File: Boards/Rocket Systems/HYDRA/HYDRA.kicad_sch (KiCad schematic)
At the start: 63 parts, among them IC1 BC846BLT1G, IC2 NSVT30010MXV6T1G, J1 Conn_01x01_Socket, J11 Conn_01x01_Socket, J12 Conn_01x01_Socket, J13 Conn_01x01_Socket, J14 Conn_01x01_Socket, J15 Conn_01x01_Socket, J16 Conn_01x01_Socket, J17 Conn_01x01_Socket, J18 Conn_01x01_Socket, J2 Conn_01x01_Socket, J3 Conn_01x01_Socket, J4 Conn_01x01_Socket, J5 Conn_01x01_Socket, J6 Conn_01x01_Socket, J8 Conn_01x01_Socket, J9 Conn_01x01_Socket, Q2 2N7002H6327XTSA2, Q3 2N7002H6327XTSA2, Q5 BC857CMB_315, Q6 BC857CMB_315, Q7 BC857CMB_315, U12 THVD2410VDRCR, U5 SQJA36EP-T1_GE3, U6 VLMKG3400-GS08, U9 SQJA36EP-T1_GE3

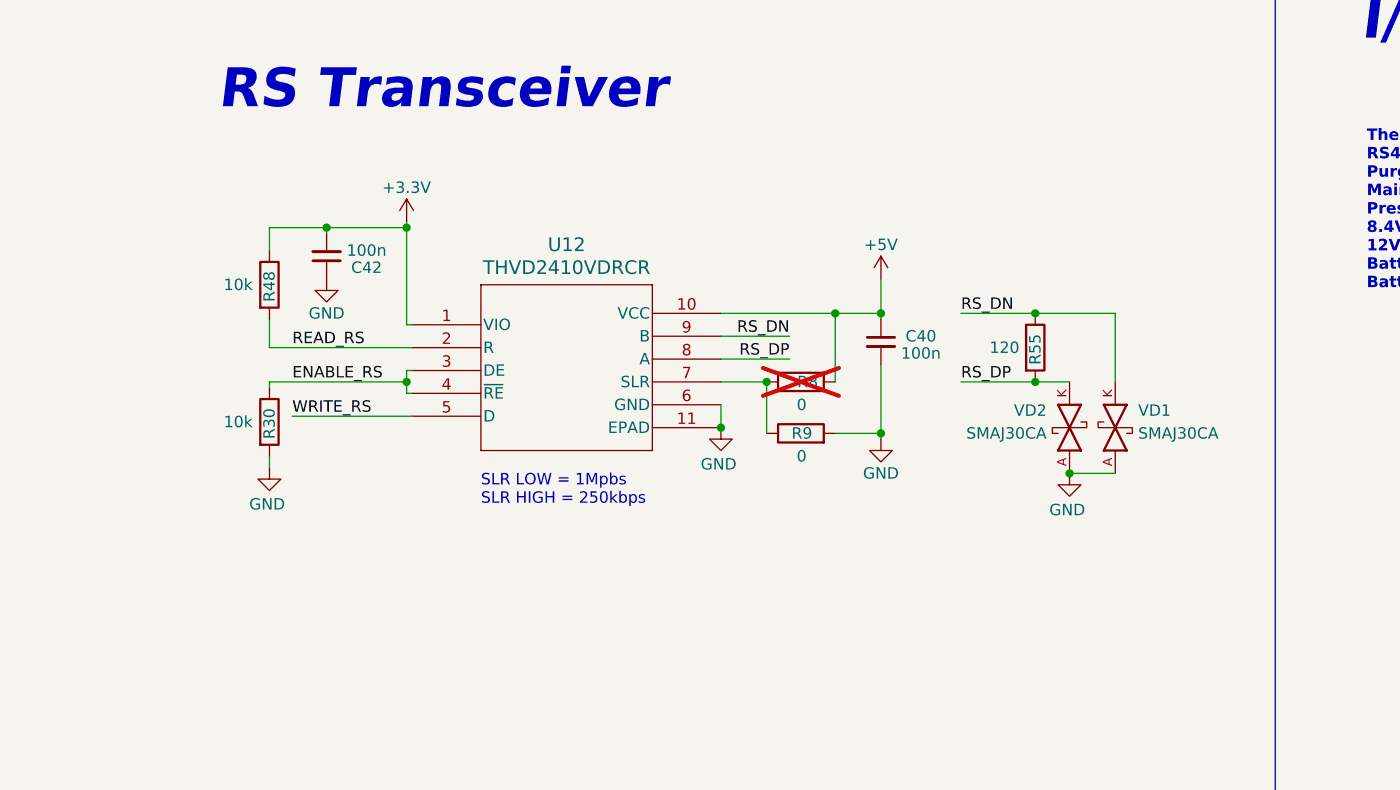
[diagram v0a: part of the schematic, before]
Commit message: OBC Full layout refactor, HYDRA Schematics UPDATE
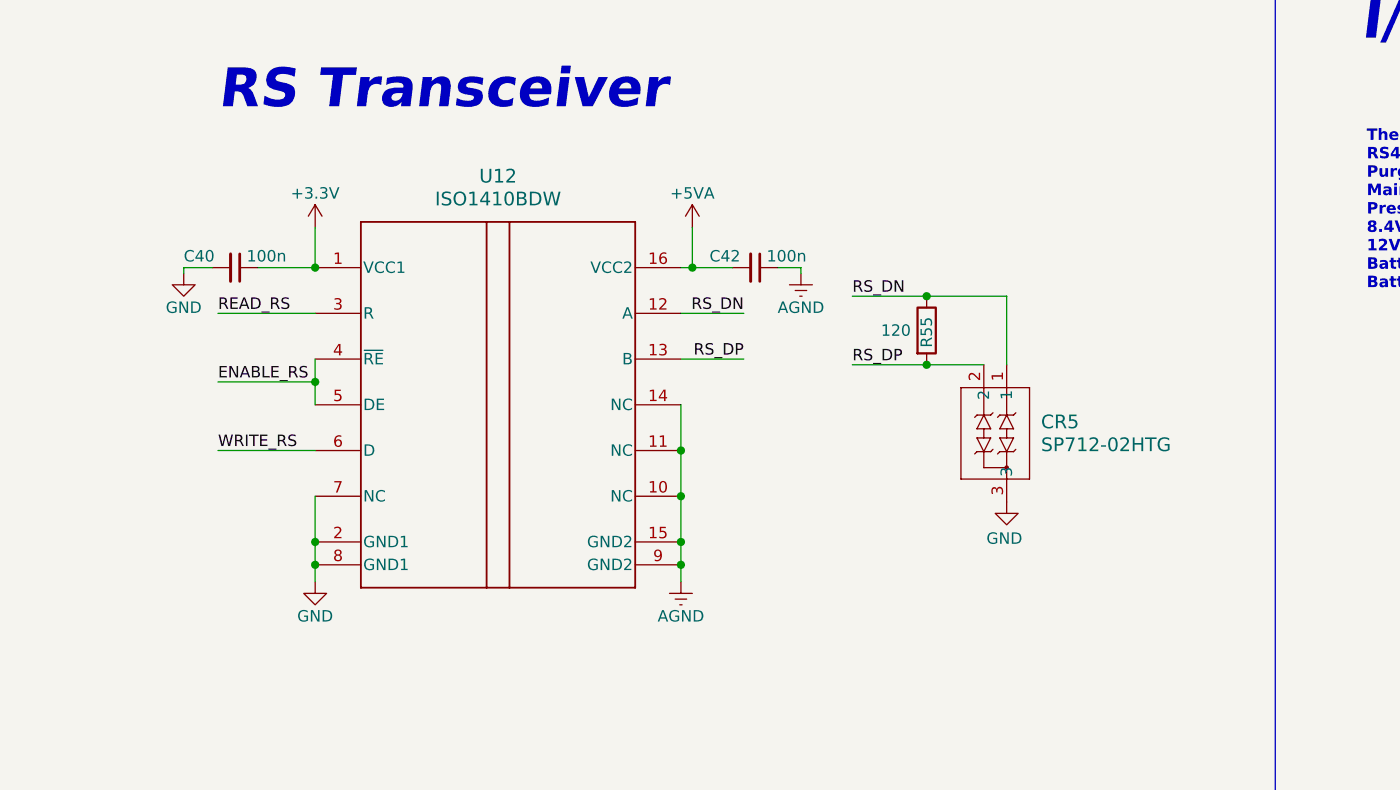
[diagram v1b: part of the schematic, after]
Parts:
- removed R30, R48: 10k, Resistor-0402:RES_0402, symbol Device:R
- removed R8, R9: 0, Resistor-0603:RES_0603, symbol Device:R
- removed U12: THVD2410VDRCR, VSON10_DRC_TEX, symbol THVD2410VDRCR:THVD2410VDRCR
- removed VD1, VD2: SMAJ30CA, symbol SMAJ30CA:SMAJ30CA
- added CR5: SP712-02HTG, 2Channel ESD RS485 - P712-02HTG:SOT23-3_LTF, symbol SP712-02HTG:SP712-02HTG
- added U12: ISO1410BDW, DW0016B_N, symbol ISO1410BDW:ISO1410BDW
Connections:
- net +3.3V: now also C40.1, U12.1 (VCC1); no longer C42.2
- net +5V: no longer C40.1
- net ENABLE_RS: now also U12.4 (~{RE}), U12.5 (DE)
- net GND: now also CR5.3, U12.2 (GND1), U12.7 (NC), U12.8 (GND1); no longer C42.1
- net READ_RS: now also U12.3 (R)
- net RS_DN: now also CR5.1, U12.12 (A)
- net RS_DP: now also CR5.2, U12.13 (B)
- net WRITE_RS: now also U12.6 (D)
- new net +5VA: C42.2, U12.16 (VCC2)
- new net AGND: C42.1, U12.10 (NC), U12.11 (NC), U12.14 (NC), U12.15 (GND2), U12.9 (GND2)
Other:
- note removed: "SLR LOW = 1Mpbs SLR HIGH = 250kbps"
- moved on the sheet: R55

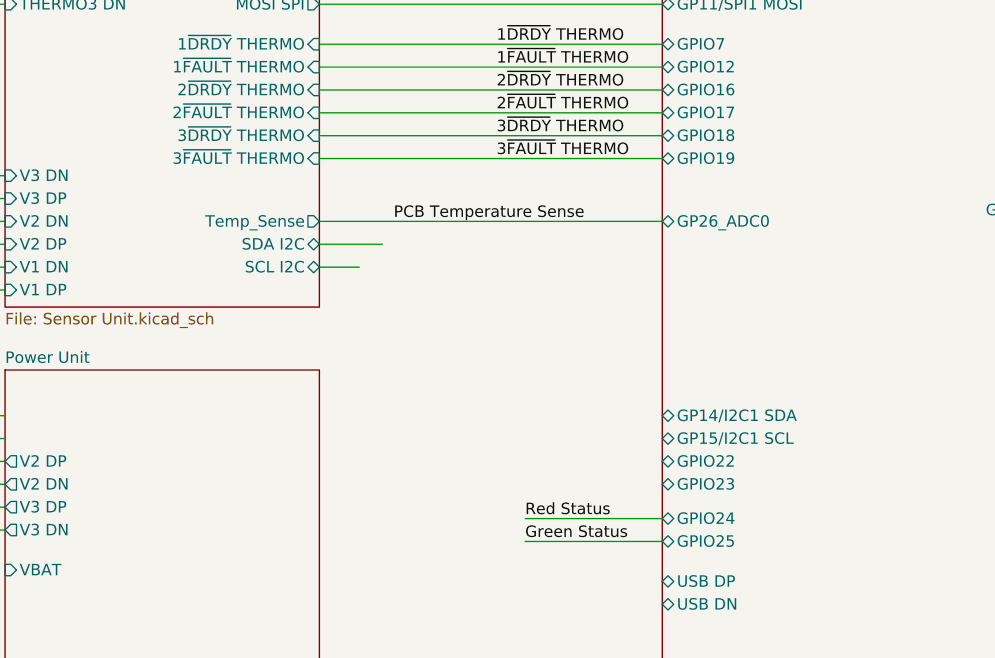
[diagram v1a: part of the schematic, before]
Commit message: updated the ADC routing in schematic
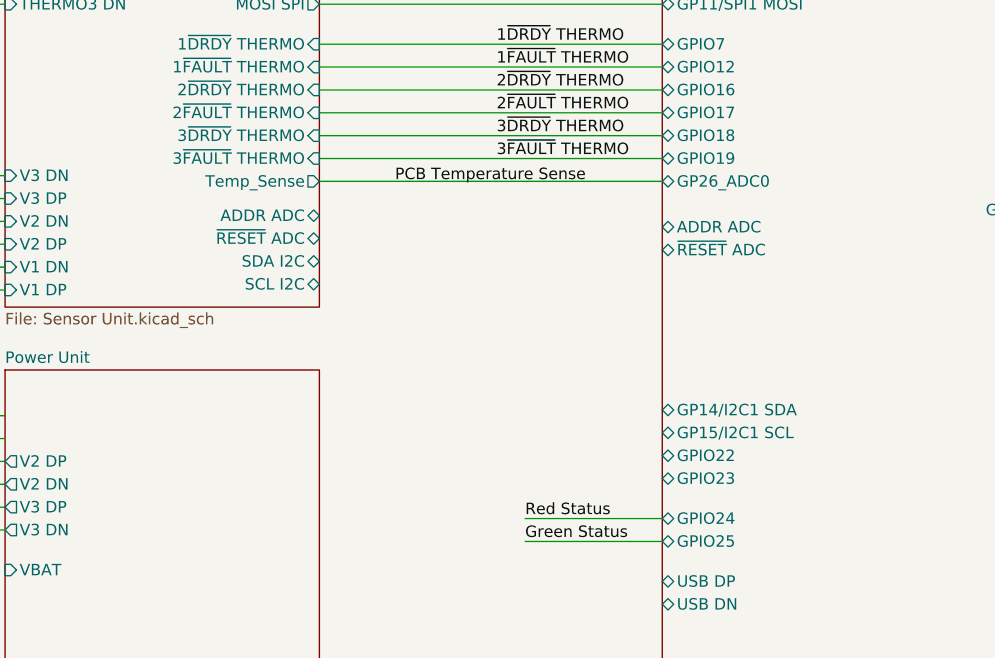
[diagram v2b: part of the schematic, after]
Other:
- sheet RP2040 Standard ports: added ADDR ADC, ~{RESET} ADC; removed none
- sheet Sensor Unit ports: added ADDR ADC, ~{RESET} ADC; removed none
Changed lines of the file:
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@@
 	(wire
 		(pts
-			(xy 100.965 100.965) (xy 105.41 100.965)
-		)
-		(stroke
-			(width 0)
-			(type default)
-		)
-	)
-	(wire
-		(pts
 			(xy 389.255 207.645) (xy 389.255 205.105)
 		)
@@
 	(wire
 		(pts
-			(xy 100.965 98.425) (xy 107.95 98.425)
-		)
-		(stroke
-			(width 0)
-			(type default)
-		)
-	)
-	(wire
-		(pts
 			(xy 251.46 74.295) (xy 251.46 79.375)
 		)
@@
 	(wire
 		(pts
-			(xy 100.965 95.885) (xy 139.065 95.885)
+			(xy 100.965 91.44) (xy 139.065 91.44)
 		)
 		(stroke
@@
 	)
 	(label "PCB Temperature Sense"
-		(at 109.22 95.885 0)
+		(at 109.3648 91.6859 0)
 		(effects
 			(font
@@
 		)
 		(pin "GPIO22" bidirectional
-			(at 139.065 122.555 180)
+			(at 139.065 121.92 180)
 			(effects
 				(font
@@
 		)
 		(pin "GP26_ADC0" bidirectional
-			(at 139.065 95.885 180)
+			(at 139.065 91.44 180)
 			(effects
 				(font
@@
 		)
 		(pin "GP15{slash}I2C1 SCL" bidirectional
-			(at 139.065 120.015 180)
+			(at 139.065 119.38 180)
 			(effects
 				(font
@@
 		)
 		(pin "GP14{slash}I2C1 SDA" bidirectional
-			(at 139.065 117.475 180)
+			(at 139.065 116.84 180)
 			(effects
 				(font
@@
 		)
 		(pin "GPIO23" bidirectional
-			(at 139.065 125.095 180)
+			(at 139.065 124.46 180)
 			(effects
 				(font
@@
 			)
 		)
+		(pin "ADDR ADC" bidirectional
+			(at 139.065 96.52 180)
+			(effects
+				(font
+					(size 1.27 1.27)
+				)
+				(justify left)
+			)
+		)
+		(pin "~{RESET} ADC" bidirectional
+			(at 139.065 99.06 180)
+			(effects
+				(font
+					(size 1.27 1.27)
+				)
+				(justify left)
+			)
+		)
 		(instances
 			(project "HYDRA"
@@
 		)
 		(pin "SDA I2C" bidirectional
-			(at 100.965 98.425 0)
+			(at 100.965 100.33 0)
 			(effects
 				(font
@@
 		)
 		(pin "SCL I2C" bidirectional
-			(at 100.965 100.965 0)
+			(at 100.965 102.87 0)
 			(effects
 				(font
@@
 		)
 		(pin "Temp_Sense" output
-			(at 100.965 95.885 0)
+			(at 100.965 91.44 0)
+			(effects
+				(font
+					(size 1.27 1.27)
+				)
+				(justify right)
+			)
+		)
+		(pin "ADDR ADC" bidirectional
+			(at 100.965 95.25 0)
+			(effects
+				(font
+					(size 1.27 1.27)
+				)
+				(justify right)
+			)
+		)
+		(pin "~{RESET} ADC" bidirectional
+			(at 100.965 97.79 0)
 			(effects
 				(font

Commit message: major changes on the HYDRA schematic including valve actuation and adc changes
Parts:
- removed D4, D7: RB095BGE-30TL, SchottkyDiode-RB095BGE:RD3P175SNFRATL, symbol RB095BGE-30TL:RB095BGE-30TL
- removed Q2, Q3: 2N7002H6327XTSA2, NMOS_2N7002:PG-SOT23-3-5_INF_MIN, symbol NMOS_2N7002:2N7002H6327XTSA2
- removed R35, R43, R57, R58: 2k, Resistor-0402:RES_0402, symbol Device:R
- removed R6, R68: 10k, Resistor-0402:RES_0402, symbol Device:R
- removed U5, U9: SQJA36EP-T1_GE3, SQJA36EP-T1-GE3:PowerPAK_SO-8L_3_VIS, symbol SQJA36EP-T1-GE3:SQJA36EP-T1_GE3
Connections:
- no-connect marks 0 -> 1
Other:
- added sheet Actuation Unit (Actuation Unit.kicad_sch)
- sheet Power Unit ports: added GNDPWR, VBAT DN, VBAT DP; removed V2 DN, V2 DP, V3 DN, V3 DP
- sheet RP2040 Standard ports: added none; removed ADDR ADC, USB DN, USB DP, ~{RESET} ADC
- sheet Sensor Unit ports: added DAC_IN1, DAC_IN2, DAC_IN3, DAC_IN4, VBAT DN, VBAT DP; removed ADDR ADC, V1 DN, V1 DP, V2 DN, V2 DP, V3 DN, V3 DP
- note added: "TODO LIST: Connectors for valves Buffer a criar Vref nos sensores de corrente Meter isto mais apresentavel Atualizar Pinout"
- note removed: "Main Valve Driver - Solenoid"
- note removed: "Purge Valve Driver - Solenoid"
- note removed: "Servo Valve Driver"
- note removed: "TODO LIST: REVER GROUNDs -> Analog, Digital, Supply LDO AGND? , USB-C PD Split AGND?, Shields nos DC.DC? Power Ground, star connection? Power Multiplexer na USB-C Buffer a criar Vref nos sensores de corrente Meter isto mais apresentavel Atualizar Pinout"
- note removed: "Valve Drivers"
- moved on the sheet: IC1, LS1, R18, R19

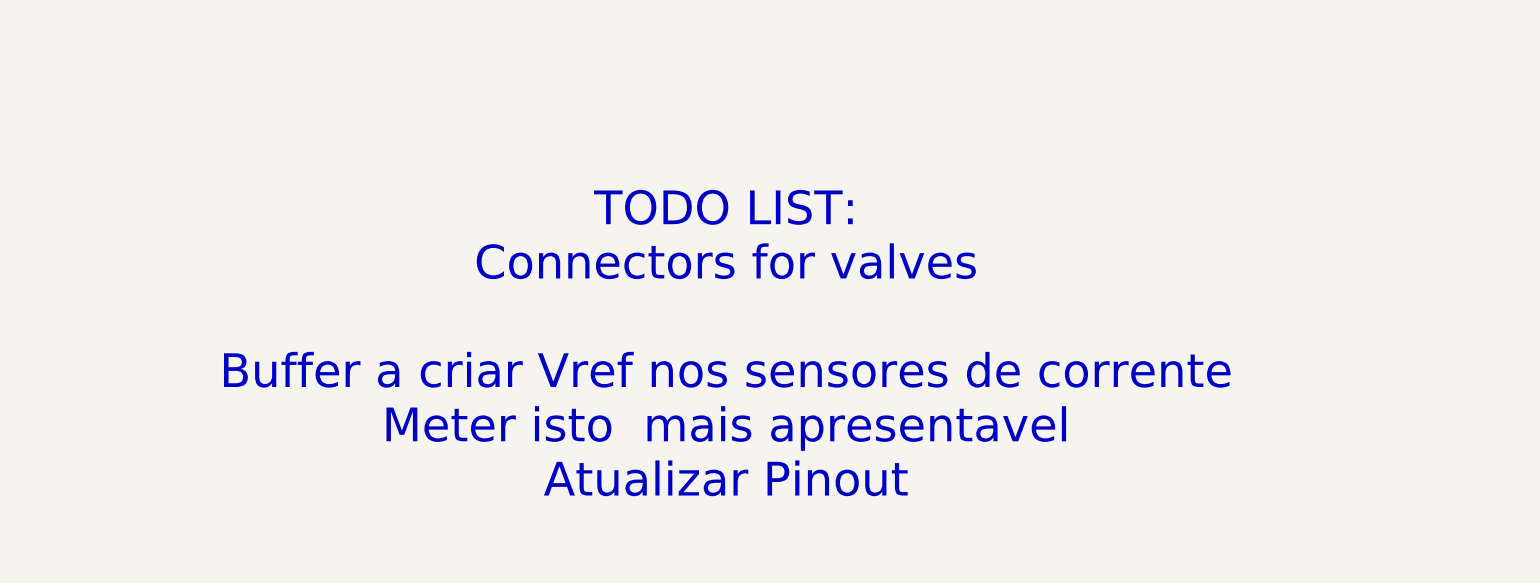
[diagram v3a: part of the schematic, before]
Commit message: Reordered the DC DC schematic
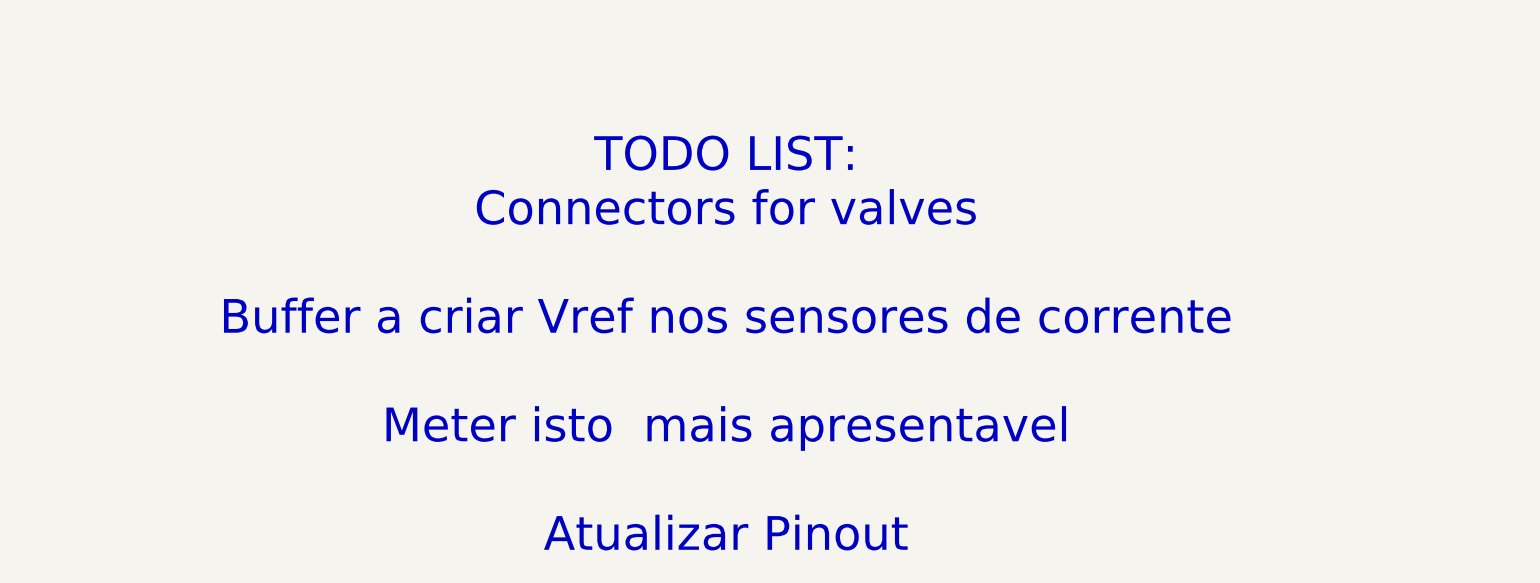
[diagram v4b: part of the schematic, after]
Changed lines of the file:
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@@
 		)
 	)
-	(text "TODO LIST:\nConnectors for valves\n\nBuffer a criar Vref nos sensores de corrente\nMeter isto  mais apresentavel \nAtualizar Pinout"
+	(text "TODO LIST:\nConnectors for valves\n\nBuffer a criar Vref nos sensores de corrente\n\nMeter isto  mais apresentavel \n\nAtualizar Pinout"
 		(exclude_from_sim no)
 		(at 136.652 352.806 0)

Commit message: Full HYDRA UPDATE
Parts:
- removed C40, C42: 100n, Capacitor-0402:Capacitor_0402, symbol Device:C_Small
- removed CR5: SP712-02HTG, 2Channel ESD RS485 - P712-02HTG:SOT23-3_LTF, symbol SP712-02HTG:SP712-02HTG
- removed J1, J11, J12, J13, J14, J15, J16, J17, J18, J2, J3, J4, J5, J6, J8, J9: Conn_01x01_Socket, Pico_Conn1x1:Pico_01pin, symbol Connector:Conn_01x01_Socket
- removed LED1, LED2, LED3: VLMS1500-GS08, LED-Red_VLMS1500-GS08:LED_00-GS08_VIS_RED, symbol VLMS1500-GS08:VLMS1500-GS08
- removed Q5, Q6, Q7: BC857CMB_315, PNP_BC857CMB_315:TRANS_PMZB550UNEYL, symbol BC857CMB_315:BC857CMB_315
- removed R29, R32, R34: 100, Resistor-0402:RES_0402, symbol Device:R
- removed R55: 120, Resistor-0603:RES_0603, symbol Device:R
- removed U12: ISO1410BDW, DW0016B_N, symbol ISO1410BDW:ISO1410BDW
- added CR1, CR3: VLMY1300-GS08, LED-Yellow_VLMY1300-GS08:LED_VISHAY_VLMX1300_VIS, symbol VLMY1300-GS08:VLMY1300-GS08
- added R1: 65, Resistor-0402:RES_0402, symbol Device:R
- added R10, R7: 10k, Resistor-0402:RES_0402, symbol Device:R
- added R3: 150, Resistor-0402:RES_0402, symbol Device:R
- renumbered CR1 to CR2, CR2 to CR4, CR3 to CR5, CR4 to CR6, IC2 to IC1, IC1 to IC2, R18 to R11, R19 to R12, R42 to R2, R31 to R4, R54 to R5, R56 to R6, R64 to R8, R67 to R9, U6 to U1
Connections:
- net +5V: now also R10.2, R7.1
- net +5VA: now also CR3.2
- net GND: now also R1.1, R3.1
- net Green Status renamed ~{Green} Status
- net ~{Green} Status: now also R7.2
- net Red Status renamed ~{Red} Status
- net ~{Red} Status: now also R10.1
- new net: CR3.1, R3.2
- new net: CR1.1, R1.2
- new net +3.3VA: CR1.2
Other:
- added sheet IO Connectors (IO Connectors.kicad_sch)
- sheet Actuation Unit ports: added ACT_N2 DUTY, ACT_N2 OUT, ACT_N2 PWR, ACT_N2 Valve, ACT_N2O DUTY, ACT_N2O OUT, ACT_N2O PWR, ACT_N2O Valve, CAM 1 IN, CAM 1 OUT, CAM 2 IN, CAM 2 OUT, CAM 3 IN, CAM 3 OUT, CAM EN, Extra Valve, Extra Valve OUT, Extra Valve PWR, QuickDisco N2, QuickDisco N2 OUT, QuickDisco N2 PWR, QuickDisco N2O, QuickDisco N2O OUT, QuickDisco N2O PWR, Servo_IN1 PWM, Servo_IN2 PWM, Servo_OUT1 PWM, Servo_OUT2 PWM, VENT_N2 DUTY, VENT_N2 OUT, VENT_N2 PWR, VENT_N2 Valve, VENT_N2O DUTY, VENT_N2O OUT, VENT_N2O PWR, VENT_N2O Valve, ~{ACT_N2 FAULT}, ~{ACT_N2O FAULT}, ~{VENT_N2 FAULT}, ~{VENT_N2O FAULT}; removed DAC_IN1, DAC_IN2, DAC_IN3, DAC_IN4, Load4 +, Load4 -, Load5 -, Load6 -, Quick Disconnect 1 Solenoid, Quick Disconnect 2 Solenoid, Valve1, Valve2, Valve3, Valve4, load1 +, load1 -, load2 +, load2 -, load3 +, load3 -, load5 +, load6 +
- sheet Power Unit ports: added GNDBAT, SERVO OUT, SERVO PWR; removed GNDPWR
- sheet RP2040 Standard ports: added GP2/PWM1 A; removed GPIO2
- sheet Sensor Unit ports: added DAC_OUT1, DAC_OUT2, DAC_OUT3, DAC_OUT4, ENABLE_RS, PRESSURE1 Sense, PRESSURE2 Sense, PRESSURE3 Sense, READ_RS, RS_DN, RS_DP, WRITE_RS, ~{ACT_N2 FAULT}, ~{ACT_N2O FAULT}, ~{FAULT ADC}, ~{VENT_N2 FAULT}, ~{VENT_N2O FAULT}; removed 1~{FAULT} THERMO, 2~{FAULT} THERMO, 3~{FAULT} THERMO, DAC_IN1, DAC_IN2, DAC_IN3, DAC_IN4
- note added: "TODO: Escolher connectores Filtros Anti-aliasing ADC FAULT DESIGN ATUALIZAR PROJECT SYMBOLS LIB ADICIONAR FOOTPRINTS CORRER ERC -- LAYOUT"
- note removed: "I/O Connectors"
- note removed: "I2C Fast Mode should be set around 400kHz. USB-C PD I2C ADDR is 0x08. ADS1115 I2C ADDR is 0x90. Higher frequencies may sink too much current. The total current sunk by the RP2040 in all GPIOs must be below 50mA"
- note removed: "RP2040 Connections"
- note removed: "RS Transceiver"
- note removed: "THERMO FAULT"
- note removed: "TODO LIST: Connectors for valves Buffer a criar Vref nos sensores de corrente Meter isto mais apresentavel Atualizar Pinout"
- note removed: "Tem de se escolher contactos apropriados para os termocouples!"
- note removed: "Temporarily assign PicoSocket as footprint. After layout design select adequate connectors."
- note removed: "Thermocouples - 3 Differential Connections (6) - INPUTs -> To Type-K probes RS485 Transceiver - 1 Differential Connection (2) - INPUT/OUTPUT Purge Valve Drive - 1 Connection - INPUT Main Valve PWM Signal Control - 1 Connection - OUTPUT Pressure Sensor Signal Input - 1 Connection - INPUT 8.4V Power Line - 1 Connection - Power Input -> Servo Motors 12V Power Line - 1 Connection - Power Input -> Pre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"
- moved on the sheet: CR2, CR4, CR5, CR6, IC1, IC2, LS1, R11, R12, R2, R4, R5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

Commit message: IO connectors
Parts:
- removed LS1: PKLCS1212E20A0-R1, PKLCS1212E20A0-R1:PKLCS1212E20A0-R1, symbol PKLCS1212E20A0-R1:PKLCS1212E20A0-R1
- added LS1: PKMCS0909E4000-R1, PKMCS0909E4000-R1:SPKR_PKMCS0909E4000-R1, symbol PKMCS0909E4000-R1:PKMCS0909E4000-R1
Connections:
- net +5V: now also LS1.1
- net at IC2.3 (C), R12.2: now also LS1.2
- no-connect marks 1 -> 0
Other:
- sheet RP2040 Standard ports: added GPIO28; removed GP28_ADC2
